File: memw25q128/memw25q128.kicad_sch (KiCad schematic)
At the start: 15 parts, among them J1 STM32WORLD_BASE, U1 W25Q128JVS

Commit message: Hmmmm
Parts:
- U1: value W25Q128JVS -> (none); footprint Package_SO:SOIC-8_5.275x5.275mm_P1.27mm -> (none)
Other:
- company: (none) -> ${COMPANY}
- title: (none) -> ${TITLE}
- moved on the sheet: C1, JP1, JP10, JP11, JP12, JP2, JP3, JP4, JP5, JP6, JP7, JP8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

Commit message: Playing with ordering files
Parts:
- U1: value (none) -> W25Q128JVS; footprint (none) -> Package_SO:SOIC-8_5.275x5.275mm_P1.27mm
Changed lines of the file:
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@@
     (rev "${REVISION}")
     (company "${COMPANY}")
-    (comment 1 "${AUTHOR_EMAIL}")
+    (comment 1 "${URL}")
     (comment 2 "${AUTHOR}")
+    (comment 3 "${AUTHOR_EMAIL}")
   )
   (junction (at 147.32 172.72) (diameter 0) (color 0 0 0 0)
@@
     (in_bom yes) (on_board yes)
     (property "Reference" "U1" (id 0) (at 83.82 76.2 0))
-    (property "Value" "" (id 1) (at 100.33 76.2 0))
-    (property "Footprint" "" (id 2) (at 92.71 85.09 0)
-      (effects (font (size 1.27 1.27)) hide)
-    )
+    (property "Value" "W25Q128JVS" (id 1) (at 100.33 76.2 0))
+    (property "Footprint" "Package_SO:SOIC-8_5.275x5.275mm_P1.27mm" (id 2) (at 92.71 85.09 0)
+      (effects (font (size 1.27 1.27)) hide)
+    )

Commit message: memw25q128 order files done and working
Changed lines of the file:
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@@
     (stroke (width 0) (type default) (color 0 0 0 0))
   )
-  (polyline (pts (xy 20.32 182.88) (xy 168.91 182.88))
+  (polyline (pts (xy 20.32 182.88) (xy 173.355 182.88))
     (stroke (width 0) (type default) (color 0 0 0 0))
   )
@@
     (stroke (width 0) (type default) (color 0 0 0 0))
   )
-  (polyline (pts (xy 20.32 190.5) (xy 168.91 190.5))
+  (polyline (pts (xy 20.32 190.5) (xy 173.355 190.5))
     (stroke (width 0) (type default) (color 0 0 0 0))
   )
@@
     (stroke (width 0) (type default) (color 0 0 0 0))
   )
-  (polyline (pts (xy 168.91 167.64) (xy 168.91 190.5))
+  (polyline (pts (xy 173.355 167.64) (xy 173.355 190.5))
     (stroke (width 0) (type default) (color 0 0 0 0))
   )
@@
     (stroke (width 0) (type default) (color 0 0 0 0))
   )
-  (polyline (pts (xy 20.32 167.64) (xy 168.91 167.64))
+  (polyline (pts (xy 20.32 167.64) (xy 173.355 167.64))
     (stroke (width 0) (type default) (color 0 0 0 0))
   )
@@
     (stroke (width 0) (type default) (color 0 0 0 0))
   )
-  (polyline (pts (xy 20.32 175.26) (xy 168.91 175.26))
-    (stroke (width 0) (type default) (color 0 0 0 0))
-  )
+  (polyline (pts (xy 20.32 175.26) (xy 173.355 175.26))
+    (stroke (width 0) (type default) (color 0 0 0 0))
+  )

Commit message: Hmmmm
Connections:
- net +3V3: no longer J1.1 (3.3V), J1.79 (3.3V)
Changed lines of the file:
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@@
   (junction (at 92.71 62.23) (diameter 0) (color 0 0 0 0)
   )
-  (junction (at 228.6 35.56) (diameter 0) (color 0 0 0 0)
-  )
   (junction (at 251.46 139.7) (diameter 0) (color 0 0 0 0)
   )
@@
   (junction (at 110.49 172.72) (diameter 0) (color 0 0 0 0)
   )
-  (junction (at 228.6 93.98) (diameter 0) (color 0 0 0 0)
-  )
   (junction (at 73.66 180.34) (diameter 0) (color 0 0 0 0)
   )
@@
     (stroke (width 0) (type default) (color 0 0 0 0))
   )
-  (wire (pts (xy 228.6 35.56) (xy 228.6 81.28))
-    (stroke (width 0) (type default) (color 0 0 0 0))
-  )
   (wire (pts (xy 251.46 142.24) (xy 251.46 139.7))
     (stroke (width 0) (type default) (color 0 0 0 0))
@@
     (stroke (width 0) (type default) (color 0 0 0 0))
   )
-  (wire (pts (xy 228.6 33.02) (xy 228.6 35.56))
+  (wire (pts (xy 228.6 33.02) (xy 228.6 81.28))
     (stroke (width 0) (type default) (color 0 0 0 0))
   )
@@
     (stroke (width 0) (type default) (color 0 0 0 0))
   )
-  (wire (pts (xy 228.6 93.98) (xy 228.6 139.7))
+  (wire (pts (xy 228.6 81.28) (xy 228.6 139.7))
     (stroke (width 0) (type default) (color 0 0 0 0))
   )
@@
     (stroke (width 0) (type default) (color 0 0 0 0))
   )
-  (wire (pts (xy 228.6 93.98) (xy 231.14 93.98))
-    (stroke (width 0) (type default) (color 0 0 0 0))
-  )
   (wire (pts (xy 86.36 172.72) (xy 88.9 172.72))
     (stroke (width 0) (type default) (color 0 0 0 0))
@@
     (stroke (width 0) (type default) (color 0 0 0 0))
   )
-  (wire (pts (xy 228.6 81.28) (xy 228.6 93.98))
-    (stroke (width 0) (type default) (color 0 0 0 0))
-  )
   (wire (pts (xy 226.06 66.04) (xy 231.14 66.04))
     (stroke (width 0) (type default) (color 0 0 0 0))
@@
     (stroke (width 0) (type default) (color 0 0 0 0))
   )
-  (wire (pts (xy 228.6 35.56) (xy 231.14 35.56))
-    (stroke (width 0) (type default) (color 0 0 0 0))
-  )

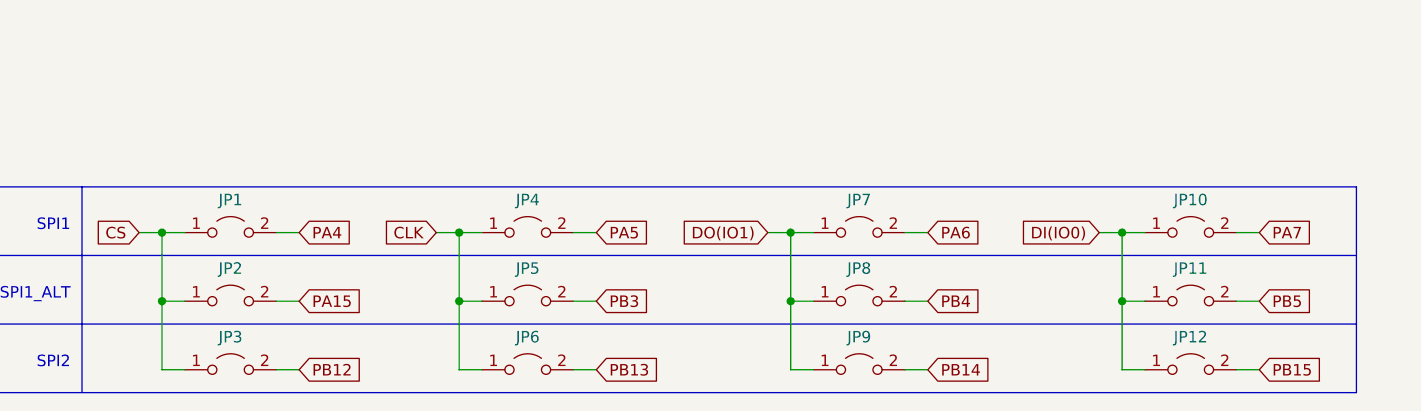
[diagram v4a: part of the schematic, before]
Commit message: Changed jumpers on memw25qxx
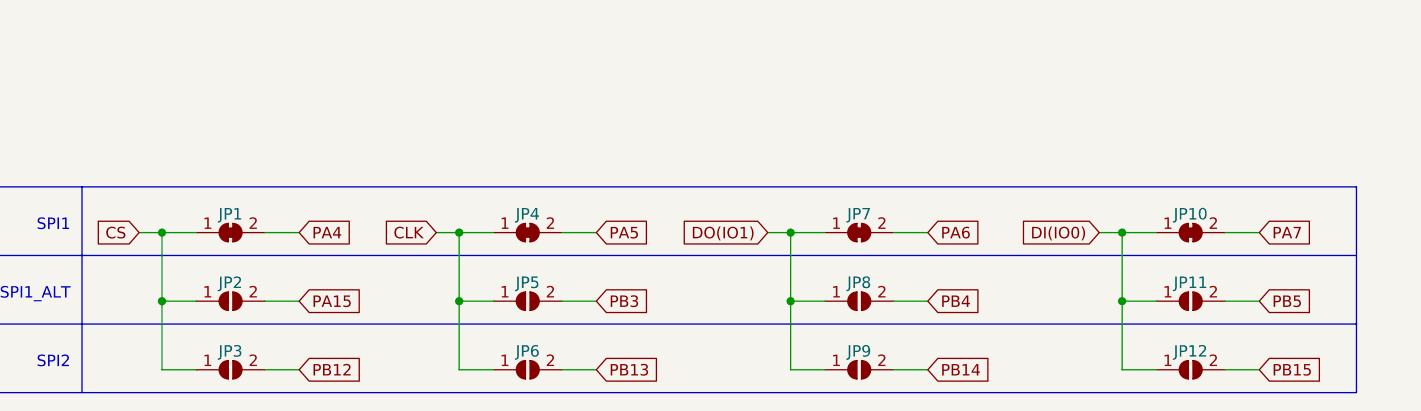
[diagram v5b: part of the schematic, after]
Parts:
- removed JP1, JP10, JP11, JP12, JP2, JP3, JP4, JP5, JP6, JP7, JP8, JP9: ~, Jumper:SolderJumper-2_P1.3mm_Open_RoundedPad1.0x1.5mm, symbol Jumper:Jumper_2_Open
- added JP1, JP10, JP4, JP7: SolderJumper_2_Bridged, Jumper:SolderJumper-2_P1.3mm_Bridged_RoundedPad1.0x1.5mm, symbol stm32world:SolderJumper_2_Bridged
- added JP11, JP12, JP2, JP3, JP5, JP6, JP8, JP9: SolderJumper_2_Open, Jumper:SolderJumper-2_P1.3mm_Open_RoundedPad1.0x1.5mm, symbol stm32world:SolderJumper_2_Open
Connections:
- net CLK: now also JP4.1 (A), JP5.1 (A), JP6.1 (A)
- net CS: now also JP1.1 (A), JP2.1 (A), JP3.1 (A)
- net DI(IO0): now also JP10.1 (A), JP11.1 (A), JP12.1 (A)
- net DO(IO1): now also JP7.1 (A), JP8.1 (A), JP9.1 (A)
- net PA15: now also JP2.2 (B)
- net PA4: now also JP1.2 (B)
- net PA5: now also JP4.2 (B)
- net PA6: now also JP7.2 (B)
- net PA7: now also JP10.2 (B)
- net PB12: now also JP3.2 (B)
- net PB13: now also JP6.2 (B)
- net PB14: now also JP9.2 (B)
- net PB15: now also JP12.2 (B)
- net PB3: now also JP5.2 (B)
- net PB4: now also JP8.2 (B)
- net PB5: now also JP11.2 (B)

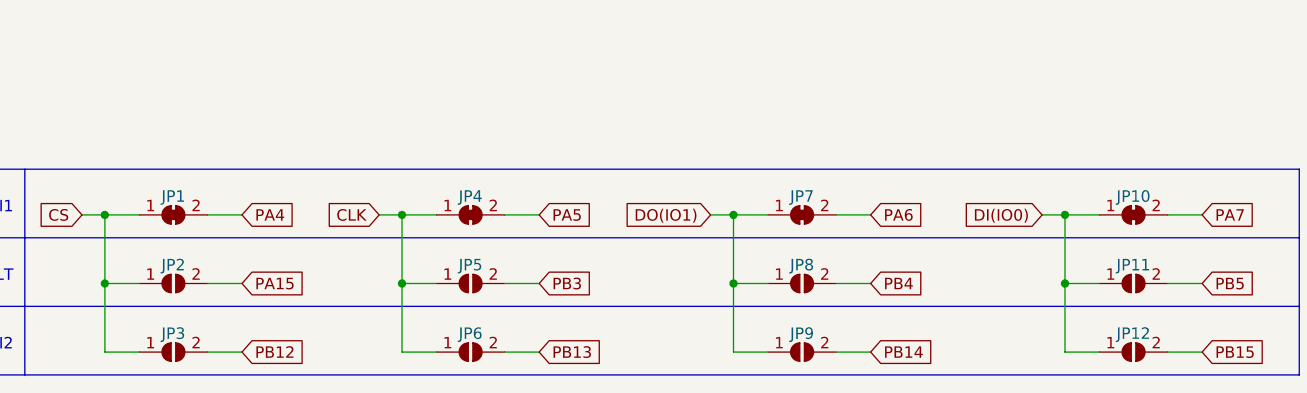
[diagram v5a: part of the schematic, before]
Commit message: mem25q128 ready to order
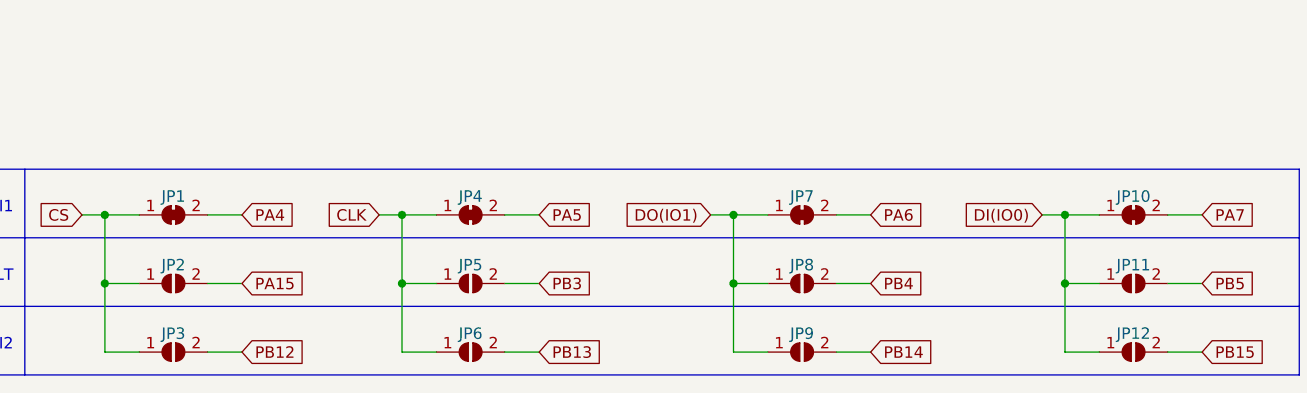
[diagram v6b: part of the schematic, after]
